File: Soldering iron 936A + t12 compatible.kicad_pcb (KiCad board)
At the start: 2 copper layers, 97 x 67 mm, 109 parts, among them J1 DC INPUT, J2 USB TO SERIAL, J3 AC input, J4 output_connector, J5 mosfet_driver_future_backup, J6 OLED, J7 USB C BREAKOUT BOARD, Q1 IRF9540N, Q2 BC547, SW1 RotaryEncoder_Switch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

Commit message: Checked all errors , fixed whatever was possible only clearance error's exist , now have to check warnings
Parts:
- R31: moved to B.Cu
- moved C1 4.23 mm to (191.2, 128.2), turned to -90 degrees
- moved C12 0.25 mm to (261.8, 98.0)
- moved R31 0.25 mm to (259.8, 98.5)
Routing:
- net /thermocouple_t12 +: track 8.94 -> 16.4 mm
- net /ENCODER S: track 76.8 -> 78.9 mm
- net +5V: track 238.7 -> 240.2 mm, vias 19 -> 20

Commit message: Added , placed refernce , next have to check warnings , silkscreen
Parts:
- added C27: 100nf, Capacitor_SMD:C_0603_1608Metric_Pad1.08x0.95mm_HandSolder, B.Cu at (188.4, 80.8)
- added C28: 100nf, Capacitor_SMD:C_0603_1608Metric_Pad1.08x0.95mm_HandSolder, B.Cu at (188.4, 75.2)
- added U6: REF3040, Package_TO_SOT_SMD:SOT-23, B.Cu at (188.6, 78.0)
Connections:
- A1 pad 18: unconnected-(A1-AREF-Pad18) -> /4.096V_REF
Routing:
- net GND: track 107.1 -> 112.8 mm
- net /4.096V_REF: track 0.00 -> 5.02 mm
- net +5V: track 240.2 -> 242.1 mm, vias 20 -> 21
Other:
- board text added: "Soldering Iron V5.1 AC"
- board text removed: "Soldering Iron V5 AC"

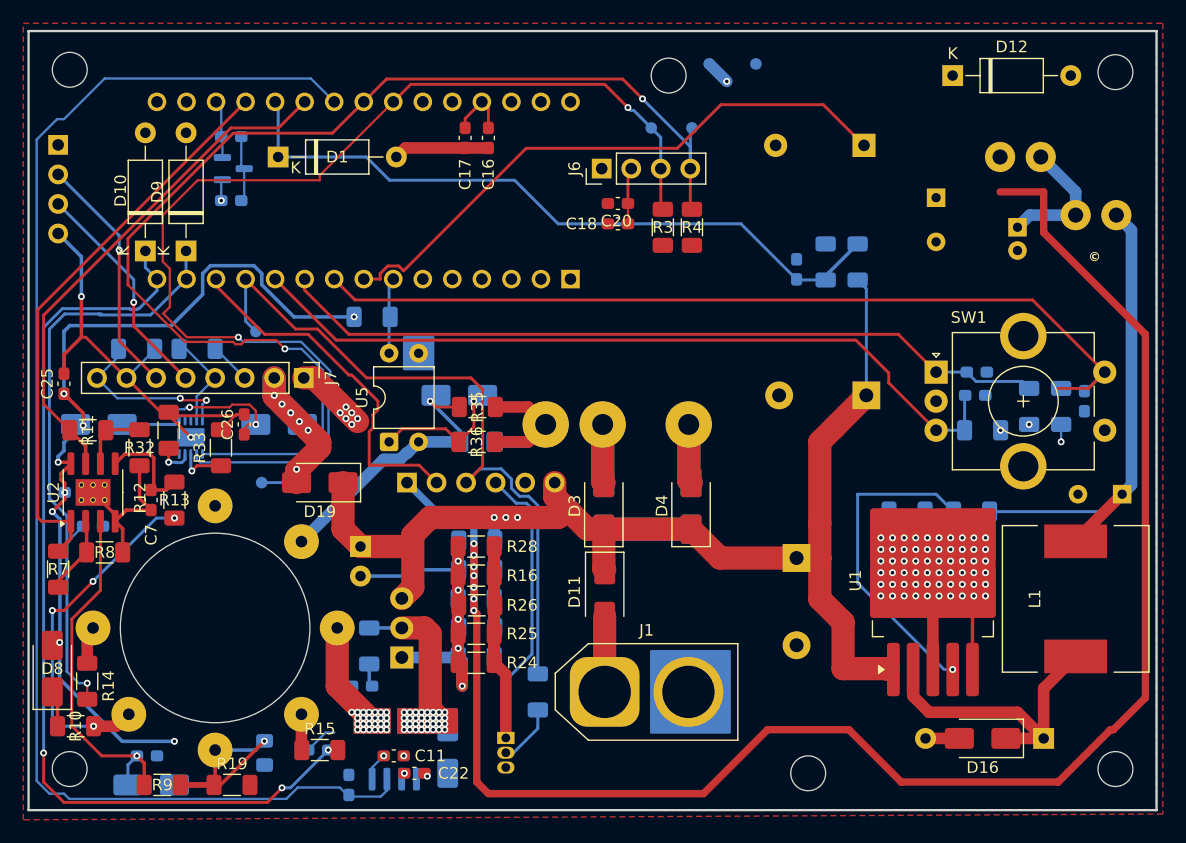
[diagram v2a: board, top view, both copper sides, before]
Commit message: Review few of the warnings
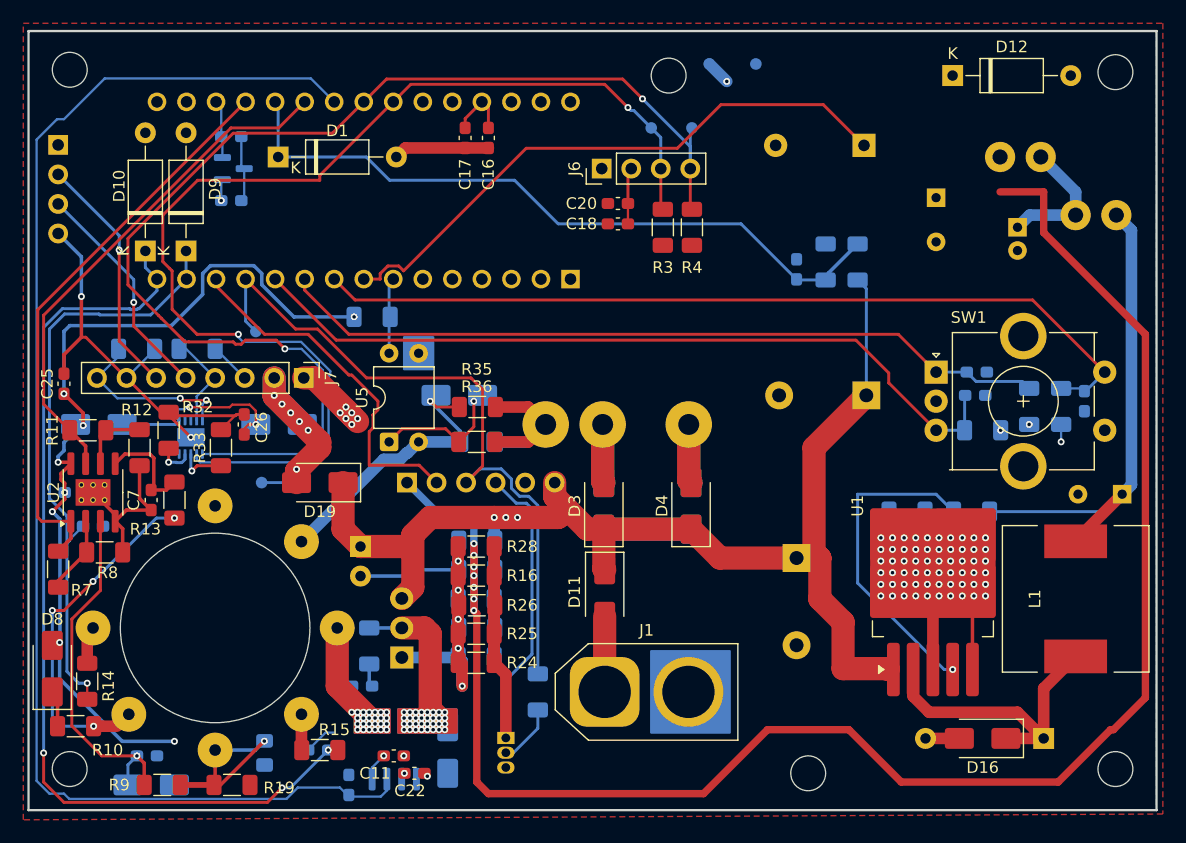
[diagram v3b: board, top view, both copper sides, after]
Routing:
- net /ENCODER S: track 78.9 -> 74.4 mm
- net /SCL: track 100.2 -> 99.2 mm
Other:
- board text added: "EARTH"
- board text added: "GND"
- board text added: "P+"
- board text added: "SB"
- board text added: "SS"
- board text added: "T_A1560+"
- board text added: "T_T12+"

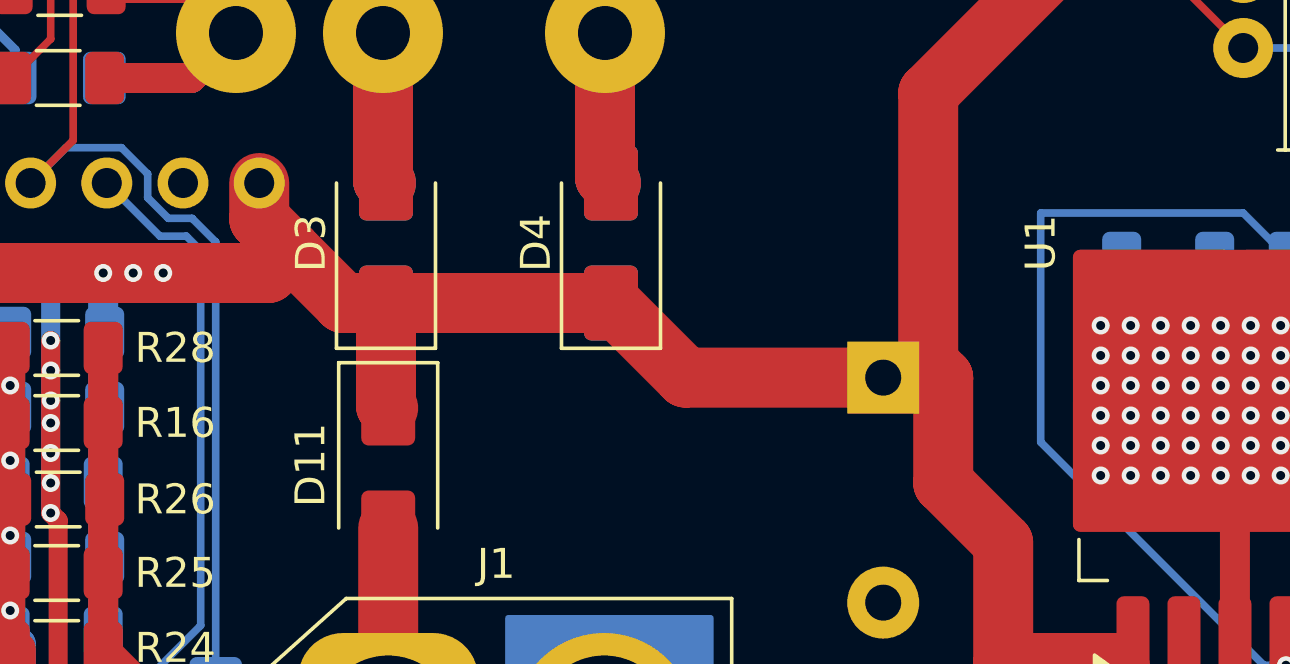
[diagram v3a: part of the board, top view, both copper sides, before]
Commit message: only warnings are left to see , will now try slots cutting for type c
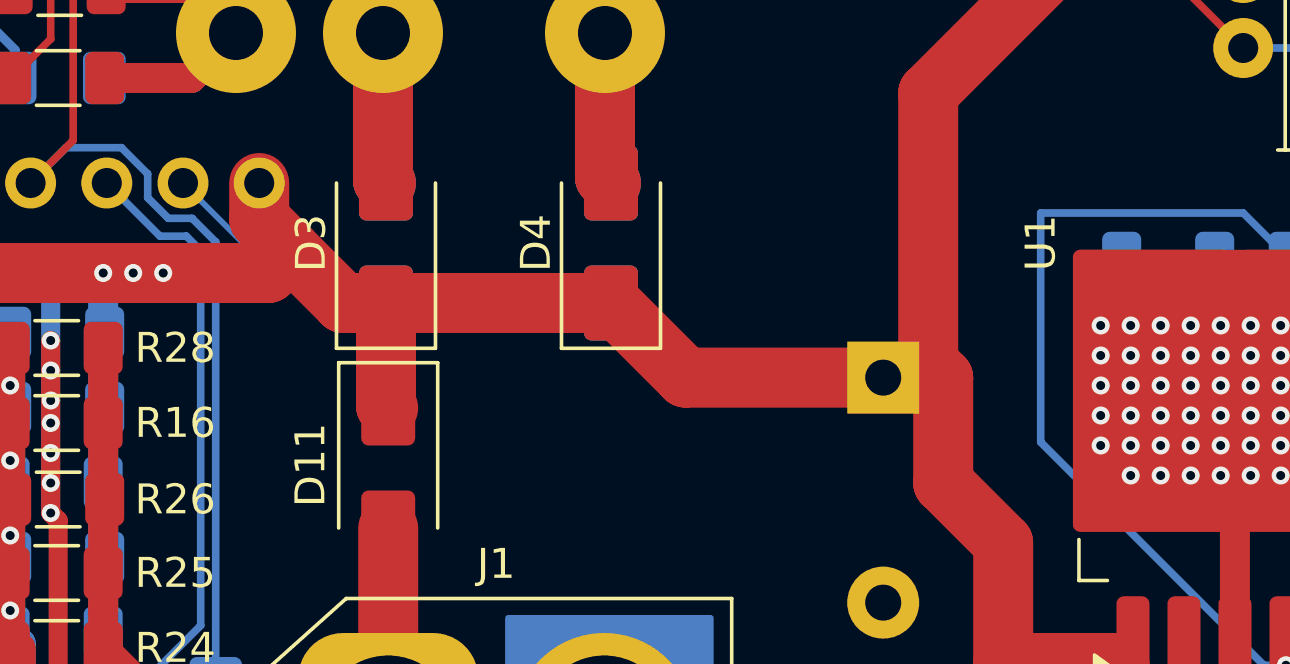
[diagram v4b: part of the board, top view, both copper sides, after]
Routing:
- net GND: track 112.8 -> 121.2 mm, vias 70 -> 69
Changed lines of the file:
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@@
 		(model "${KICAD9_3DMODEL_DIR}/Connector_PinHeader_2.54mm.3dshapes/PinHeader_1x08_P2.54mm_Horizontal.wrl"
 			(offset
-				(xyz -1.25 0 4)
+				(xyz -1.25 0 2.65)
 			)
 			(scale
@@
 		(model "${KIPRJMOD}/micro usb C Adafruit 4090 - corrected.STEP"
 			(offset
-				(xyz -2 -4.75 15.5)
+				(xyz -2 -4.75 14)
 			)
 			(scale
@@
 	)
 	(via
-		(at 244.25 114.75)
-		(size 0.6)
-		(drill 0.3)
-		(layers "F.Cu" "B.Cu")
-		(net 4)
-	)
-	(via
 		(at 245.25 112.75)
 		(size 0.6)
@@
 	)
 	(segment
+		(start 215.66 107)
+		(end 217.25 107)
+		(width 0.2)
+		(layer "B.Cu")
+		(net 4)
+	)
+	(segment
+		(start 217.25 107)
+		(end 219.25 109)
+		(width 0.2)
+		(layer "B.Cu")
+		(net 4)
+	)
+	(segment
 		(start 195 128)
 		(end 196.5 126.5)
@@
 	)
 	(segment
+		(start 219.25 109)
+		(end 220.425856 109)
+		(width 0.2)
+		(layer "B.Cu")
+		(net 4)
+	)
+	(segment
 		(start 220.425856 109)
 		(end 227.925856 109)
@@
 	)
 	(segment
+		(start 213.66 105)
+		(end 215.66 107)
+		(width 0.2)
+		(layer "B.Cu")
+		(net 4)
+	)
+	(segment
 		(start 175.5 89)
 		(end 175.5 85.58)
@@
 		(polygon
 			(pts
-				(xy 212 96) (xy 204.5 96) (xy 204.5 100.25) (xy 201 100.25) (xy 200.75 100.5) (xy 200.75 103.25)
-				(xy 212 103.25)
+				(xy 212.75 95.75) (xy 204 95.75) (xy 204 100.001961) (xy 200.515625 100.015625) (xy 200.5 100) (xy 200.5 103.25)
+				(xy 212.75 103.25)
 			)
 		)
@@
 			)
 		)
+	)
+	(zone
+		(net 0)
+		(net_name "")
+		(layer "B.Cu")
+		(hatch edge 0.5)
+		(connect_pads
+			(clearance 0)
+		)
+		(min_thickness 0.25)
+		(filled_areas_thickness no)
+		(keepout
+			(tracks allowed)
+			(vias allowed)
+			(pads allowed)
+			(copperpour not_allowed)
+			(footprints allowed)
+		)
+		(placement
+			(enabled no)
+			(sheetname "/")
+		)
+		(fill
+			(thermal_gap 0.5)
+			(thermal_bridge_width 0.5)
+		)
+		(polygon
+			(pts
+				(xy 212.75 103) (xy 218.75 103) (xy 218.75 96.75) (xy 212.75 96.75)
+			)
+		)

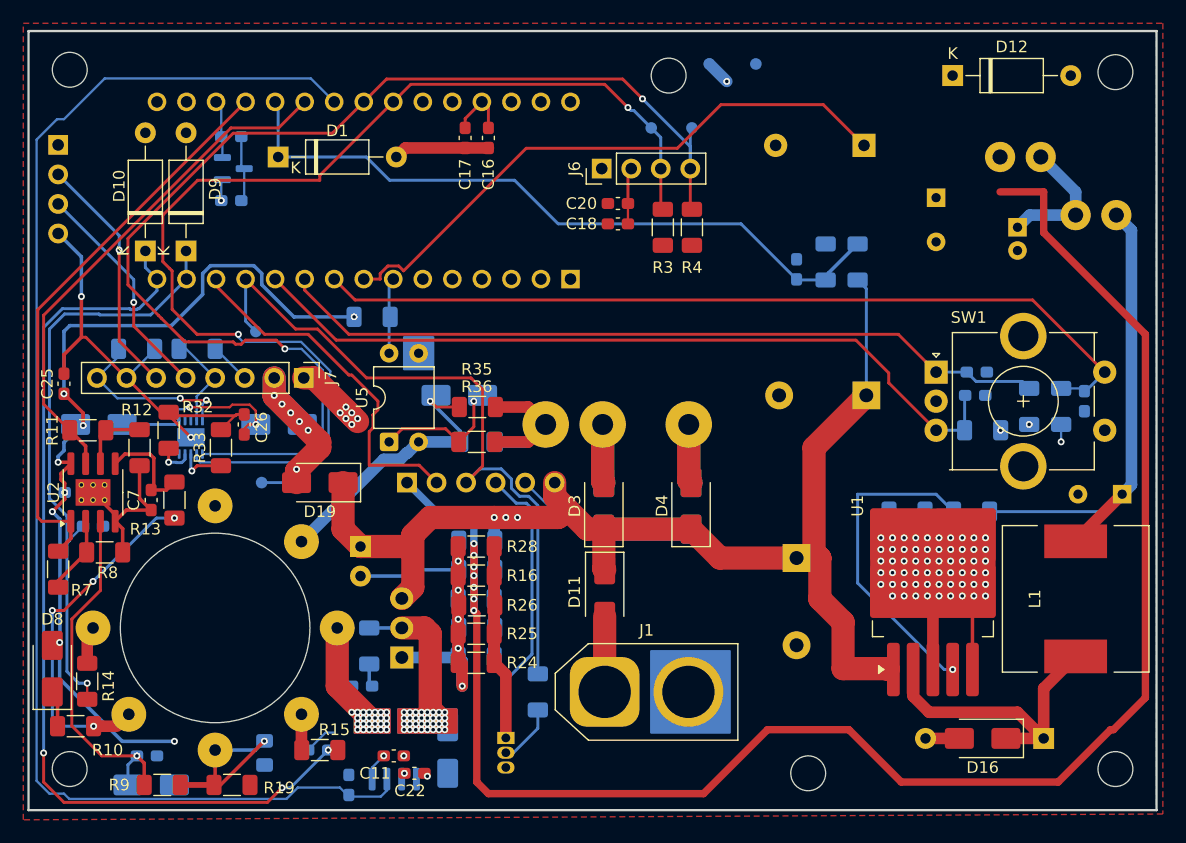
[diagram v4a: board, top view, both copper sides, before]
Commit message: Added cut for the type C board , differential roting pending
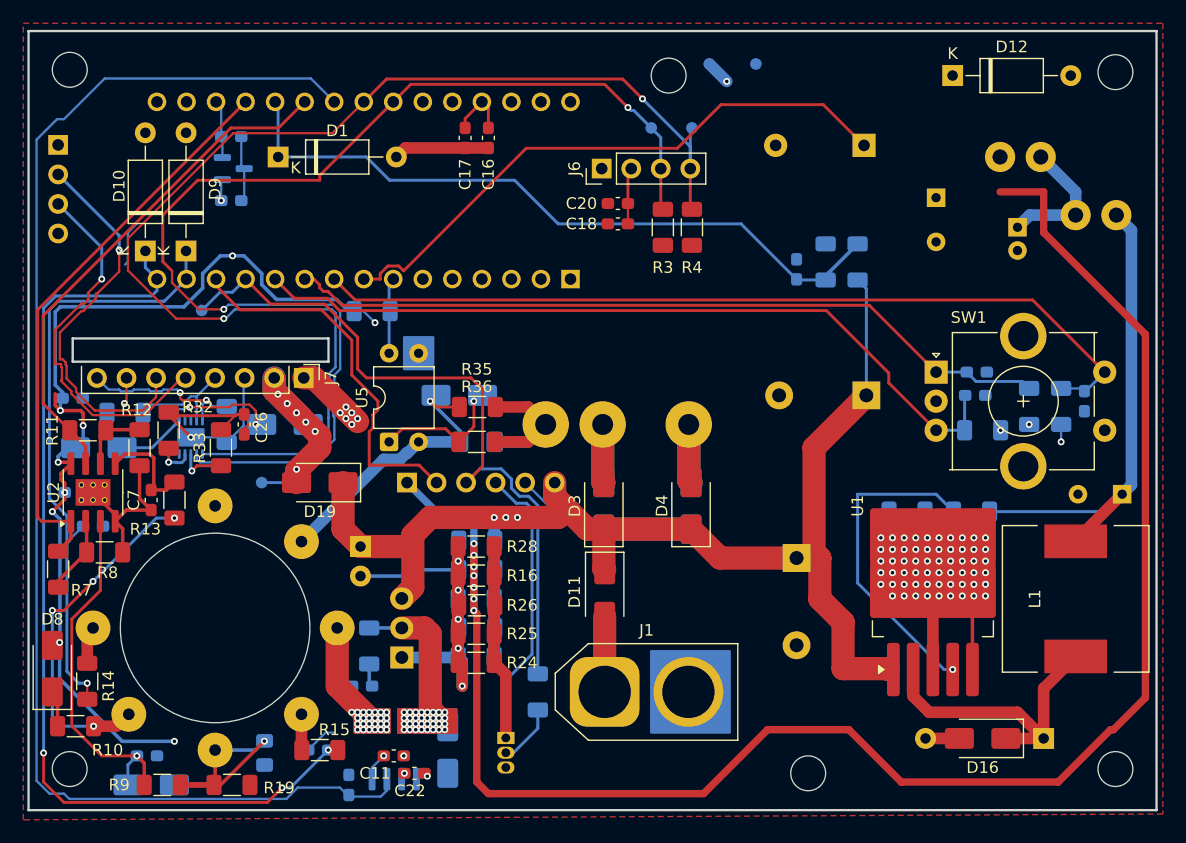
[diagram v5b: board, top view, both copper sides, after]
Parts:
- C25: moved to B.Cu
- moved R34 10.1 mm to (188.0, 100.0), turned to 90 degrees
- moved R38 8.29 mm to (179.2, 99.0), turned to 0 degrees
- moved PWM1 4.99 mm to (185.8, 90.2)
- moved D7 2.00 mm to (177.0, 102.0)
- moved C25 1.46 mm to (174.8, 97.8), turned to 0 degrees
- moved D17 0.50 mm to (193.0, 100.0)
- moved R37 0.50 mm to (200.5, 90.2)
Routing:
- net GND: track 121.2 -> 106.5 mm
- net /D-: track 19.5 -> 32.5 mm
- net /D+: track 21.0 -> 33.5 mm
- net +5V: track 242.1 -> 249.5 mm, vias 21 -> 22
- net /SDA: track 106.6 -> 110.7 mm
- net /SCL: track 99.2 -> 102.4 mm
- net /PWM1: track 30.8 -> 32.6 mm
- net /PWM: track 60.7 -> 62.3 mm
- net Net-(D17-K): track 15.5 -> 16.8 mm
- net /CC1: track 8.46 -> 9.52 mm
- net Net-(A1-D12): track 81.9 -> 82.8 mm
- net Net-(A1-D11): track 51.8 -> 52.7 mm
- net /CC2: track 15.4 -> 14.6 mm
- net /VIN_USBC: track 20.1 -> 19.5 mm
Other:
- outline, holes or cut-outs redrawn

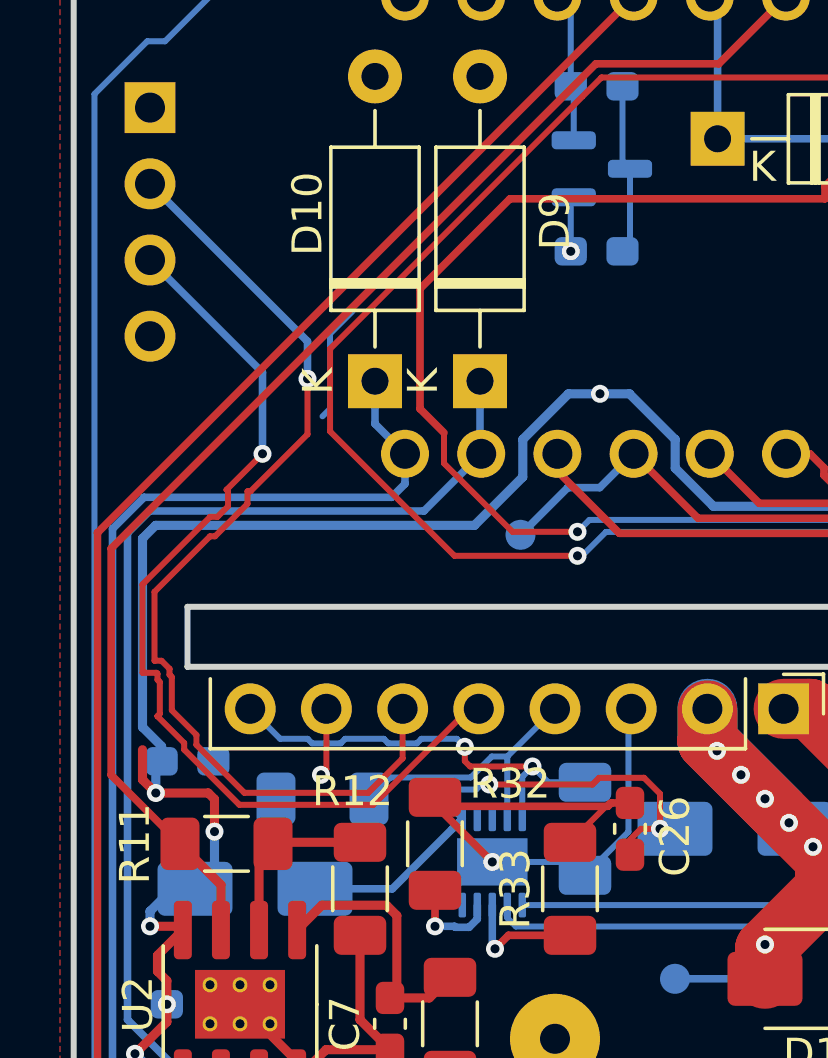
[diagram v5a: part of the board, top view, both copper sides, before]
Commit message: Length matched the usb data traces
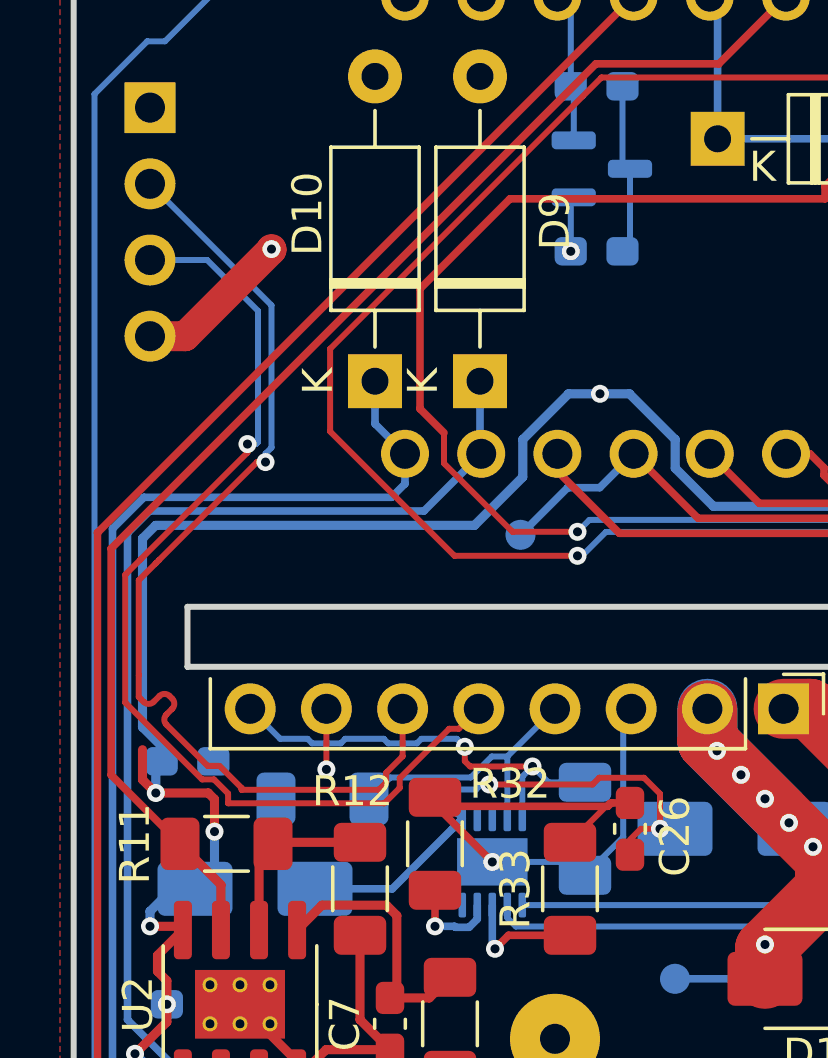
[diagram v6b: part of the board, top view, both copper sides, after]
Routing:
- net /D-: track 32.5 -> 34.2 mm
- net GND: track 106.5 -> 107.6 mm, vias 69 -> 70
- net /D+: track 33.5 -> 34.2 mm
